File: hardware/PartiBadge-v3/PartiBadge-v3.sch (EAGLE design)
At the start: 24 parts, among them J1 I2C, J2 Supply, T1 BC850

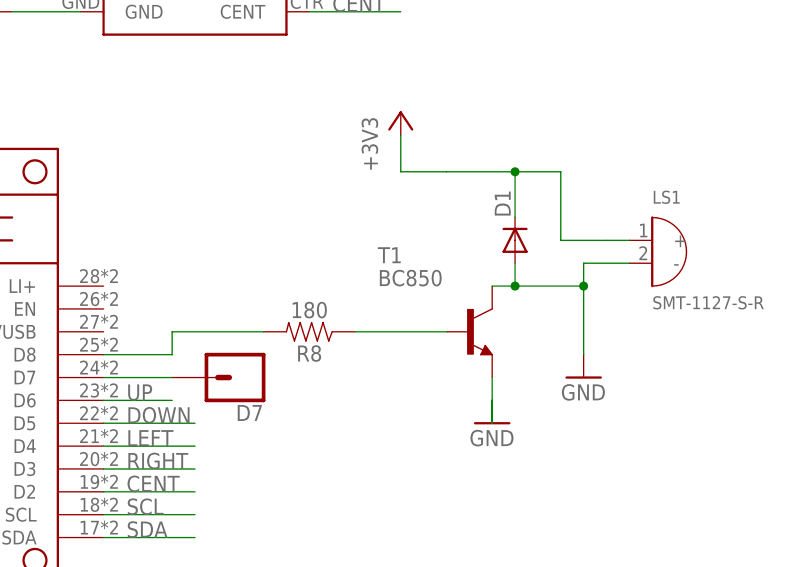
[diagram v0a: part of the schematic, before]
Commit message: swapped out npn transistor
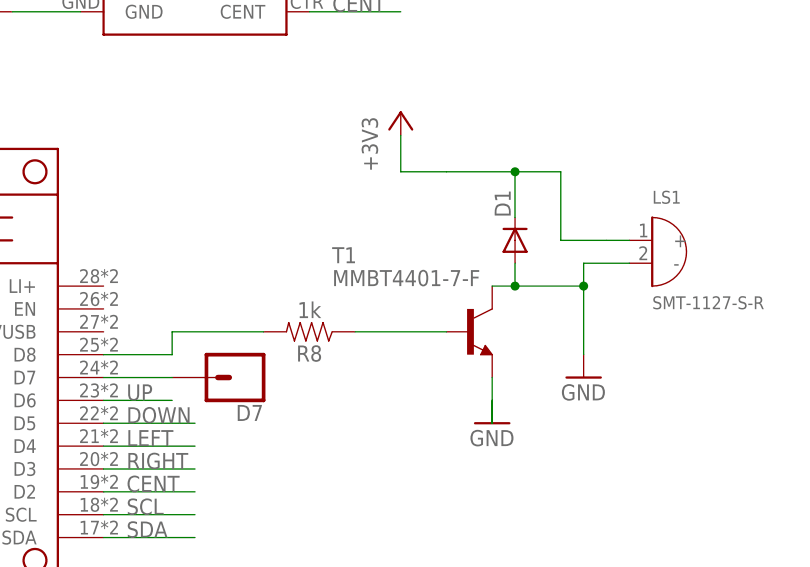
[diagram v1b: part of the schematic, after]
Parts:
- R8: value 180 -> 1k
- T1: value BC850 -> MMBT4401-7-F; device transistor:BC850 -> transistor:MMBT4401LT1-NPN-SOT23-BEC
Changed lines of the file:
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@@
 <part name="D7" library="SparkFun-Connectors" library_urn="urn:adsk.eagle:library:513" deviceset="CONN_01" device="" package3d_urn="urn:adsk.eagle:package:38028/1"/>
 <part name="MS1" library="Particle-Mesh" deviceset="PARTICLE_MESH" device="_SMTDUAL"/>
-<part name="T1" library="transistor" library_urn="urn:adsk.eagle:library:402" deviceset="BC850" device="" package3d_urn="urn:adsk.eagle:package:29904/2"/>
 <part name="D1" library="diode" library_urn="urn:adsk.eagle:library:210" deviceset="DIODE-" device="SOD323-W" package3d_urn="urn:adsk.eagle:package:43418/1"/>
-<part name="R8" library="SparkFun-Resistors" library_urn="urn:adsk.eagle:library:532" deviceset="10KOHM" device="-0603-1/10W-1%" package3d_urn="urn:adsk.eagle:package:39650/1" value="180"/>
+<part name="R8" library="SparkFun-Resistors" library_urn="urn:adsk.eagle:library:532" deviceset="10KOHM" device="-0603-1/10W-1%" package3d_urn="urn:adsk.eagle:package:39650/1" value="1k"/>
 <part name="+3V3" library="supply1" library_urn="urn:adsk.eagle:library:371" deviceset="+3V3" device=""/>
 <part name="GND8" library="supply1" library_urn="urn:adsk.eagle:library:371" deviceset="GND" device=""/>
 <part name="LS1" library="SMT-1127-S-R" deviceset="SMT-1127-S-R" device=""/>
+<part name="T1" library="transistor" library_urn="urn:adsk.eagle:library:402" deviceset="*-NPN-" device="SOT23-BEC" package3d_urn="urn:adsk.eagle:package:28748/2" technology="MMBT4401LT1" value="MMBT4401-7-F"/>
 </parts>
 <sheets>
@@
 <instance part="D7" gate="G$1" x="86.36" y="50.8" rot="R180"/>
 <instance part="MS1" gate="G$1" x="33.02" y="27.94"/>
-<instance part="T1" gate="G$1" x="111.76" y="55.88"/>
 <instance part="D1" gate="G$1" x="116.84" y="66.04" rot="R90"/>
 <instance part="R8" gate="G$1" x="93.98" y="55.88" rot="R180"/>
@@
 <instance part="GND8" gate="1" x="114.3" y="45.72"/>
 <instance part="LS1" gate="G$1" x="132.08" y="66.04"/>
+<instance part="T1" gate="G$1" x="111.76" y="55.88" smashed="yes">
+<attribute name="NAME" x="96.52" y="63.5" size="1.778" layer="95"/>
+<attribute name="VALUE" x="96.52" y="60.96" size="1.778" layer="96"/>
+</instance>
 </instances>
 <busses>
@@
 <pinref part="GND8" gate="1" pin="GND"/>
 <wire x1="114.3" y1="45.72" x2="114.3" y2="48.26" width="0.1524" layer="91"/>
+<wire x1="114.3" y1="50.8" x2="114.3" y2="45.72" width="0.1524" layer="91"/>
 <pinref part="T1" gate="G$1" pin="E"/>
-<wire x1="114.3" y1="50.8" x2="114.3" y2="45.72" width="0.1524" layer="91"/>
-</segment>
-<segment>
-<pinref part="T1" gate="G$1" pin="C"/>
+</segment>
+<segment>
 <wire x1="114.3" y1="60.96" x2="116.84" y2="60.96" width="0.1524" layer="91"/>
 <wire x1="116.84" y1="60.96" x2="124.46" y2="60.96" width="0.1524" layer="91"/>
@@
 <pinref part="LS1" gate="G$1" pin="-"/>
 <wire x1="124.46" y1="63.5" x2="129.54" y2="63.5" width="0.1524" layer="91"/>
+<pinref part="T1" gate="G$1" pin="C"/>
 </segment>
 </net>
@@
 <segment>
 <pinref part="R8" gate="G$1" pin="1"/>
+<wire x1="99.06" y1="55.88" x2="109.22" y2="55.88" width="0.1524" layer="91"/>
 <pinref part="T1" gate="G$1" pin="B"/>
-<wire x1="99.06" y1="55.88" x2="109.22" y2="55.88" width="0.1524" layer="91"/>
-</segment>
-</net>
+</segment>
+</net>

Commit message: finished Xenon port
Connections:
- new net N$18: D1.A, T1.C
- net GND: no longer D1.A, T1.C
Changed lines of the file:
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@@
 </segment>
 <segment>
-<wire x1="114.3" y1="60.96" x2="116.84" y2="60.96" width="0.1524" layer="91"/>
-<wire x1="116.84" y1="60.96" x2="124.46" y2="60.96" width="0.1524" layer="91"/>
-<pinref part="D1" gate="G$1" pin="A"/>
-<wire x1="116.84" y1="63.5" x2="116.84" y2="60.96" width="0.1524" layer="91"/>
-<junction x="116.84" y="60.96"/>
 <pinref part="GND3" gate="1" pin="GND"/>
-<wire x1="124.46" y1="60.96" x2="124.46" y2="53.34" width="0.1524" layer="91"/>
-<wire x1="124.46" y1="60.96" x2="124.46" y2="63.5" width="0.1524" layer="91"/>
-<junction x="124.46" y="60.96"/>
+<wire x1="124.46" y1="63.5" x2="124.46" y2="53.34" width="0.1524" layer="91"/>
 <pinref part="LS1" gate="G$1" pin="-"/>
 <wire x1="124.46" y1="63.5" x2="129.54" y2="63.5" width="0.1524" layer="91"/>
-<pinref part="T1" gate="G$1" pin="C"/>
 </segment>
 </net>
@@
 </segment>
 </net>
+<net name="N$18" class="0">
+<segment>
+<pinref part="D1" gate="G$1" pin="A"/>
+<wire x1="116.84" y1="63.5" x2="116.84" y2="60.96" width="0.1524" layer="91"/>
+<wire x1="114.3" y1="60.96" x2="116.84" y2="60.96" width="0.1524" layer="91"/>
+<pinref part="T1" gate="G$1" pin="C"/>
+</segment>
+</net>

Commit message: piezo tweak from Frank
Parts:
- added R7: 33R, SparkFun-Resistors:10KOHM-0603-1/10W-1%
- added U$1, U$2: SPARK_LOGO_WITH_PLANE, Spark:SPARK_LOGO_WITH_PLANE
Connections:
- new net N$20: D1.C, LS1.+, R7.1
- net +3V3: now also R7.2; no longer D1.C, LS1.+
- net GND: no longer LS1.-
- net N$18: now also LS1.-
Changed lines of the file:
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@@
 <part name="+3V1" library="supply1" library_urn="urn:adsk.eagle:library:371" deviceset="+3V3" device=""/>
 <part name="+3V2" library="supply1" library_urn="urn:adsk.eagle:library:371" deviceset="+3V3" device=""/>
-<part name="GND3" library="supply1" library_urn="urn:adsk.eagle:library:371" deviceset="GND" device=""/>
 <part name="+3V4" library="supply1" library_urn="urn:adsk.eagle:library:371" deviceset="+3V3" device=""/>
 <part name="GND4" library="supply1" library_urn="urn:adsk.eagle:library:371" deviceset="GND" device=""/>
@@
 <part name="LS1" library="SMT-1127-S-R" deviceset="SMT-1127-S-R" device=""/>
 <part name="T1" library="transistor" library_urn="urn:adsk.eagle:library:402" deviceset="*-NPN-" device="SOT23-BEC" package3d_urn="urn:adsk.eagle:package:28748/2" technology="MMBT4401LT1" value="MMBT4401-7-F"/>
+<part name="R7" library="SparkFun-Resistors" library_urn="urn:adsk.eagle:library:532" deviceset="10KOHM" device="-0603-1/10W-1%" package3d_urn="urn:adsk.eagle:package:39650/1" value="33R"/>
+<part name="U$1" library="Spark" deviceset="SPARK_LOGO_WITH_PLANE" device=""/>
+<part name="U$2" library="Spark" deviceset="SPARK_LOGO_WITH_PLANE" device=""/>
 </parts>
 <sheets>
@@
 <instance part="+3V1" gate="G$1" x="30.48" y="20.32"/>
 <instance part="+3V2" gate="G$1" x="63.5" y="-5.08"/>
-<instance part="GND3" gate="1" x="124.46" y="50.8"/>
 <instance part="+3V4" gate="G$1" x="127" y="20.32"/>
 <instance part="GND4" gate="1" x="127" y="5.08"/>
@@
 <instance part="D1" gate="G$1" x="116.84" y="66.04" rot="R90"/>
 <instance part="R8" gate="G$1" x="93.98" y="55.88" rot="R180"/>
-<instance part="+3V3" gate="G$1" x="104.14" y="80.264" smashed="yes"/>
+<instance part="+3V3" gate="G$1" x="101.6" y="80.264" smashed="yes"/>
 <instance part="GND8" gate="1" x="114.3" y="45.72"/>
 <instance part="LS1" gate="G$1" x="132.08" y="66.04"/>
@@
 <attribute name="VALUE" x="96.52" y="60.96" size="1.778" layer="96"/>
 </instance>
+<instance part="R7" gate="G$1" x="109.22" y="73.66" rot="R180"/>
+<instance part="U$1" gate="G$1" x="91.44" y="-2.54"/>
+<instance part="U$2" gate="G$1" x="101.6" y="-2.54"/>
 </instances>
 <busses>
@@
 <wire x1="114.3" y1="50.8" x2="114.3" y2="45.72" width="0.1524" layer="91"/>
 <pinref part="T1" gate="G$1" pin="E"/>
-</segment>
-<segment>
-<pinref part="GND3" gate="1" pin="GND"/>
-<wire x1="124.46" y1="63.5" x2="124.46" y2="53.34" width="0.1524" layer="91"/>
-<pinref part="LS1" gate="G$1" pin="-"/>
-<wire x1="124.46" y1="63.5" x2="129.54" y2="63.5" width="0.1524" layer="91"/>
 </segment>
 </net>
@@
 <segment>
 <pinref part="+3V3" gate="G$1" pin="+3V3"/>
-<wire x1="104.14" y1="77.724" x2="104.14" y2="73.66" width="0.1524" layer="91"/>
-<wire x1="104.14" y1="73.66" x2="109.22" y2="73.66" width="0.1524" layer="91"/>
+<wire x1="101.6" y1="77.724" x2="101.6" y2="73.66" width="0.1524" layer="91"/>
 <label x="101.6" y="73.66" size="1.778" layer="95" rot="R90"/>
-<pinref part="D1" gate="G$1" pin="C"/>
-<wire x1="116.84" y1="73.66" x2="116.84" y2="68.58" width="0.1524" layer="91"/>
-<wire x1="116.84" y1="73.66" x2="121.92" y2="73.66" width="0.1524" layer="91"/>
-<wire x1="121.92" y1="73.66" x2="121.92" y2="66.04" width="0.1524" layer="91"/>
-<wire x1="121.92" y1="66.04" x2="127" y2="66.04" width="0.1524" layer="91"/>
-<pinref part="LS1" gate="G$1" pin="+"/>
-<wire x1="127" y1="66.04" x2="129.54" y2="66.04" width="0.1524" layer="91"/>
-<wire x1="109.22" y1="73.66" x2="116.84" y2="73.66" width="0.1524" layer="91"/>
-<junction x="116.84" y="73.66"/>
+<pinref part="R7" gate="G$1" pin="2"/>
+<wire x1="104.14" y1="73.66" x2="101.6" y2="73.66" width="0.1524" layer="91"/>
 </segment>
 </net>
@@
 <net name="N$18" class="0">
 <segment>
+<pinref part="LS1" gate="G$1" pin="-"/>
 <pinref part="D1" gate="G$1" pin="A"/>
 <wire x1="116.84" y1="63.5" x2="116.84" y2="60.96" width="0.1524" layer="91"/>
 <wire x1="114.3" y1="60.96" x2="116.84" y2="60.96" width="0.1524" layer="91"/>
 <pinref part="T1" gate="G$1" pin="C"/>
-</segment>
-</net>
+<wire x1="129.54" y1="63.5" x2="116.84" y2="63.5" width="0.1524" layer="91"/>
+<junction x="116.84" y="63.5"/>
+</segment>
+</net>
+<net name="N$20" class="0">
+<segment>
+<pinref part="D1" gate="G$1" pin="C"/>
+<wire x1="116.84" y1="73.66" x2="116.84" y2="68.58" width="0.1524" layer="91"/>
+<wire x1="116.84" y1="73.66" x2="121.92" y2="73.66" width="0.1524" layer="91"/>
+<wire x1="121.92" y1="73.66" x2="121.92" y2="66.04" width="0.1524" layer="91"/>
+<wire x1="121.92" y1="66.04" x2="127" y2="66.04" width="0.1524" layer="91"/>
+<pinref part="LS1" gate="G$1" pin="+"/>
+<wire x1="127" y1="66.04" x2="129.54" y2="66.04" width="0.1524" layer="91"/>
+<pinref part="R7" gate="G$1" pin="1"/>
+<wire x1="114.3" y1="73.66" x2="116.84" y2="73.66" width="0.1524" layer="91"/>
+<junction x="116.84" y="73.66"/>
+</segment>
+</net>
